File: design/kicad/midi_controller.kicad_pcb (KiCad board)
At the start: 4 copper layers, 166 x 166 mm, 26 parts, among them J1 Conn_01x02_Socket, J2 Conn_01x02_Socket, J3 Conn_01x02_Socket, J4 Conn_01x02_Socket, J5 Conn_01x02_Socket, J6 Conn_01x02_Socket, J7 Conn_01x05, SW1 MIDI_Switch_Pushbutton_PV0H24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, SW2 MIDI_Switch_Pushbutton_PV0H24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, SW3 MIDI_Switch_Pushbutton_PV0H24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

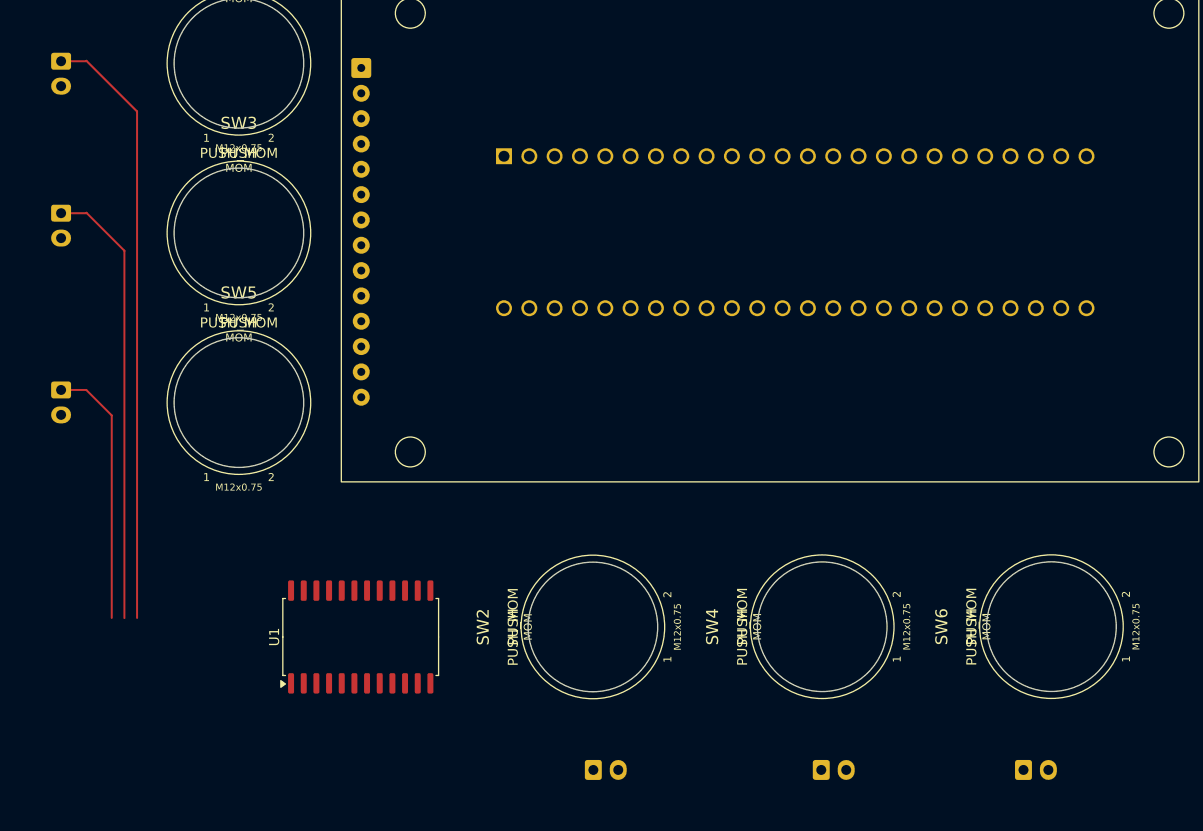
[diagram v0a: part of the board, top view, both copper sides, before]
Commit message: Update kicad binary files
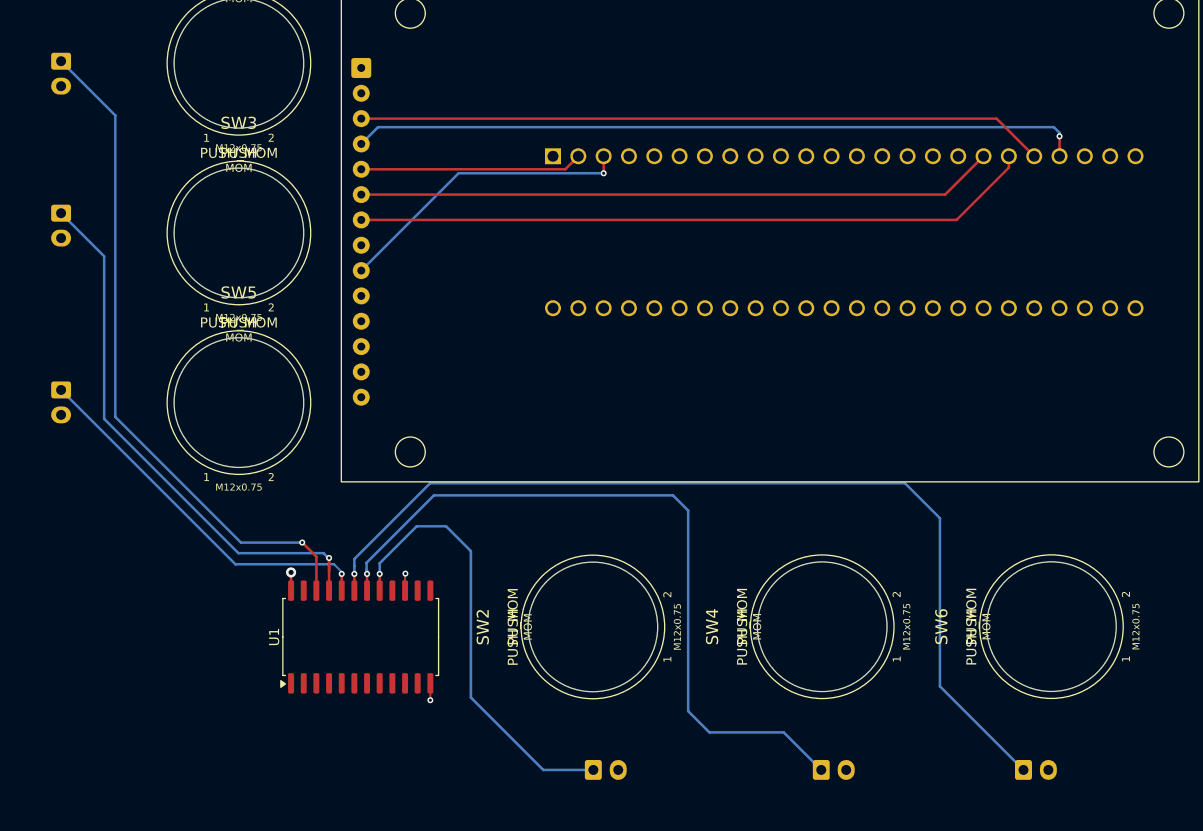
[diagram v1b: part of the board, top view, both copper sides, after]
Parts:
- moved MCU1 4.91 mm to (162.2, 107.5)
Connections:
- ENC_MECH1 pad A: /MIDI_Encoder_Matrix_2x4_with_push_buttons/1x1.QUAD_B -> /MIDI_Encoder_Matrix_2x4_with_push_buttons/1x1.QUAD_A
- ENC_MECH2 pad A: /MIDI_Encoder_Matrix_2x4_with_push_buttons/1x2.QUAD_B -> /MIDI_Encoder_Matrix_2x4_with_push_buttons/1x2.QUAD_A
- ENC_MECH3 pad A: /MIDI_Encoder_Matrix_2x4_with_push_buttons/1x3.QUAD_B -> /MIDI_Encoder_Matrix_2x4_with_push_buttons/1x3.QUAD_A
- ENC_MECH4 pad A: /MIDI_Encoder_Matrix_2x4_with_push_buttons/1x4.QUAD_B -> /MIDI_Encoder_Matrix_2x4_with_push_buttons/1x4.QUAD_A
- ENC_MECH5 pad A: /MIDI_Encoder_Matrix_2x4_with_push_buttons/2x1.QUAD_B -> /MIDI_Encoder_Matrix_2x4_with_push_buttons/2x1.QUAD_A
- ENC_MECH6 pad A: /MIDI_Encoder_Matrix_2x4_with_push_buttons/2x2.QUAD_B -> /MIDI_Encoder_Matrix_2x4_with_push_buttons/2x2.QUAD_A
- ENC_MECH7 pad A: /MIDI_Encoder_Matrix_2x4_with_push_buttons/2x3.QUAD_B -> /MIDI_Encoder_Matrix_2x4_with_push_buttons/2x3.QUAD_A
- ENC_MECH8 pad A: /MIDI_Encoder_Matrix_2x4_with_push_buttons/2x4.QUAD_B -> /MIDI_Encoder_Matrix_2x4_with_push_buttons/2x4.QUAD_A
- J7 pad 2: ENC_A_NAV -> ENC_A_OPT
- J7 pad 3: ENC_B_NAV -> ENC_B_OPT
- MCU1 pad 22: unconnected-(MCU1-30_CRX3-Pad22) -> /Encoder with Push Button_Navigation/QUAD_A
- MCU1 pad 23: unconnected-(MCU1-31_CTX3-Pad23) -> /Encoder with Push Button_Navigation/QUAD_B
- MCU1 pad 24: unconnected-(MCU1-32_OUT1B-Pad24) -> /Encoder with Push Button_Navigation/SW_A
- MCU1 pad 25: ENC_B_NAV -> ENC_A_OPT
- MCU1 pad 26: ENC_A_NAV -> ENC_B_OPT
- MCU1 pad 28: /MIDI_Encoder_Matrix_2x4_with_push_buttons/2x4.QUAD_B -> /MIDI_Encoder_Matrix_2x4_with_push_buttons/1x4.QUAD_B
- MCU1 pad 29: /MIDI_Encoder_Matrix_2x4_with_push_buttons/2x4.QUAD_B -> /MIDI_Encoder_Matrix_2x4_with_push_buttons/1x4.QUAD_A
- MCU1 pad 30: /MIDI_Encoder_Matrix_2x4_with_push_buttons/2x3.QUAD_B -> /MIDI_Encoder_Matrix_2x4_with_push_buttons/2x4.QUAD_B
- MCU1 pad 31: /MIDI_Encoder_Matrix_2x4_with_push_buttons/2x3.QUAD_B -> /MIDI_Encoder_Matrix_2x4_with_push_buttons/2x4.QUAD_A
- MCU1 pad 32: /MIDI_Encoder_Matrix_2x4_with_push_buttons/2x2.QUAD_B -> /MIDI_Encoder_Matrix_2x4_with_push_buttons/1x3.QUAD_A
- MCU1 pad 33: /MIDI_Encoder_Matrix_2x4_with_push_buttons/2x2.QUAD_B -> /MIDI_Encoder_Matrix_2x4_with_push_buttons/1x3.QUAD_B
- MCU1 pad 34: GND -> unconnected-(MCU1-GND-Pad34)
- MCU1 pad 36: /MIDI_Encoder_Matrix_2x4_with_push_buttons/2x1.QUAD_B -> /MIDI_Encoder_Matrix_2x4_with_push_buttons/2x3.QUAD_A
- MCU1 pad 37: /MIDI_Encoder_Matrix_2x4_with_push_buttons/2x1.QUAD_B -> /MIDI_Encoder_Matrix_2x4_with_push_buttons/2x3.QUAD_B
- MCU1 pad 38: /MIDI_Encoder_Matrix_2x4_with_push_buttons/1x4.QUAD_B -> /MIDI_Encoder_Matrix_2x4_with_push_buttons/2x2.QUAD_A
- MCU1 pad 39: /MIDI_Encoder_Matrix_2x4_with_push_buttons/1x4.QUAD_B -> /MIDI_Encoder_Matrix_2x4_with_push_buttons/2x2.QUAD_B
- MCU1 pad 40: /MIDI_Encoder_Matrix_2x4_with_push_buttons/1x3.QUAD_B -> /MIDI_Encoder_Matrix_2x4_with_push_buttons/1x2.QUAD_A
- MCU1 pad 41: /MIDI_Encoder_Matrix_2x4_with_push_buttons/1x3.QUAD_B -> /MIDI_Encoder_Matrix_2x4_with_push_buttons/1x2.QUAD_B
- MCU1 pad 42: /MIDI_Encoder_Matrix_2x4_with_push_buttons/1x2.QUAD_B -> /MIDI_Encoder_Matrix_2x4_with_push_buttons/2x1.QUAD_B
- MCU1 pad 43: /MIDI_Encoder_Matrix_2x4_with_push_buttons/1x2.QUAD_B -> /MIDI_Encoder_Matrix_2x4_with_push_buttons/2x1.QUAD_A
- MCU1 pad 45: /MIDI_Encoder_Matrix_2x4_with_push_buttons/1x1.QUAD_B -> /MIDI_Encoder_Matrix_2x4_with_push_buttons/1x1.QUAD_A
- U1 pad 23: /Encoder with Push Button_Navigation/SW_A -> unconnected-(U1-I8-Pad23)
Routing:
- net +5V: track 0.00 -> 159.7 mm
- net /Buttons_Momentary/BUTTON_PUSH_MOM_04: track 0.00 -> 95.2 mm, vias 0 -> 1
- net /Buttons_Momentary/BUTTON_PUSH_MOM_05: track 0.00 -> 74.4 mm, vias 0 -> 1
- net Net-(D1-RST): track 0.00 -> 73.3 mm, vias 0 -> 1
- net Net-(D1-CS): track 0.00 -> 69.1 mm
- net Net-(D1-SCK): track 0.00 -> 68.3 mm
- net Net-(D1-SDI/MOSI): track 0.00 -> 64.0 mm
- net +3V3: track 0.00 -> 63.8 mm, vias 0 -> 1
- net /Buttons_Momentary/BUTTON_PUSH_MOM_06: track 0.00 -> 44.4 mm, vias 0 -> 1
- net Net-(D1-SDO/MISO): track 0.00 -> 30.1 mm, vias 0 -> 1
- net Net-(D1-DC): track 0.00 -> 22.3 mm
- net /Buttons_Momentary/BUTTON_PUSH_MOM_03: track 26.5 -> 37.6 mm, vias 0 -> 1
- net /Buttons_Momentary/BUTTON_PUSH_MOM_02: track 44.8 -> 54.9 mm, vias 0 -> 1
- net /Buttons_Momentary/BUTTON_PUSH_MOM_01: track 60.5 -> 67.3 mm, vias 0 -> 1
- net GND: track 0.00 -> 3.42 mm, vias 0 -> 2

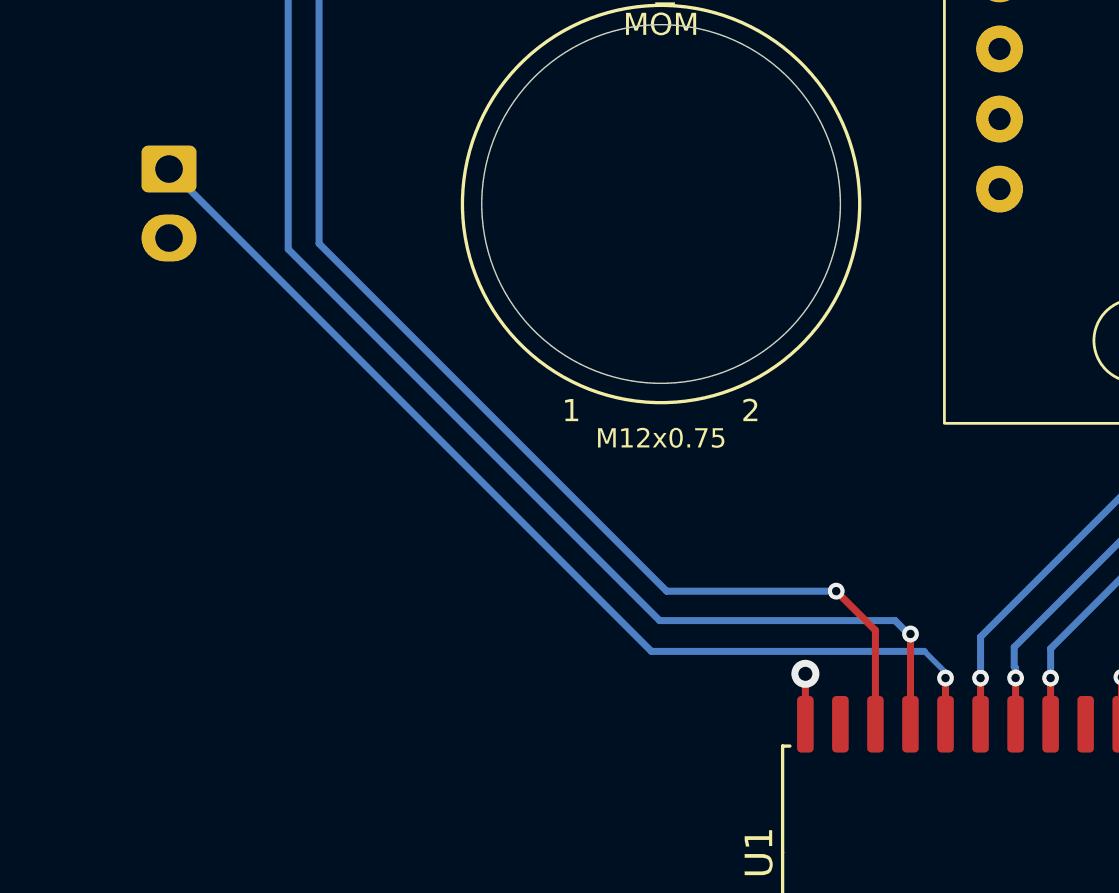
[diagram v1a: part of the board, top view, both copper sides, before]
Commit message: Refactor MIDI controller design files: updated active layer, adjusted hidden nets, and modified junction coordinates in schematic. Enhanced layout for better clarity and organization.
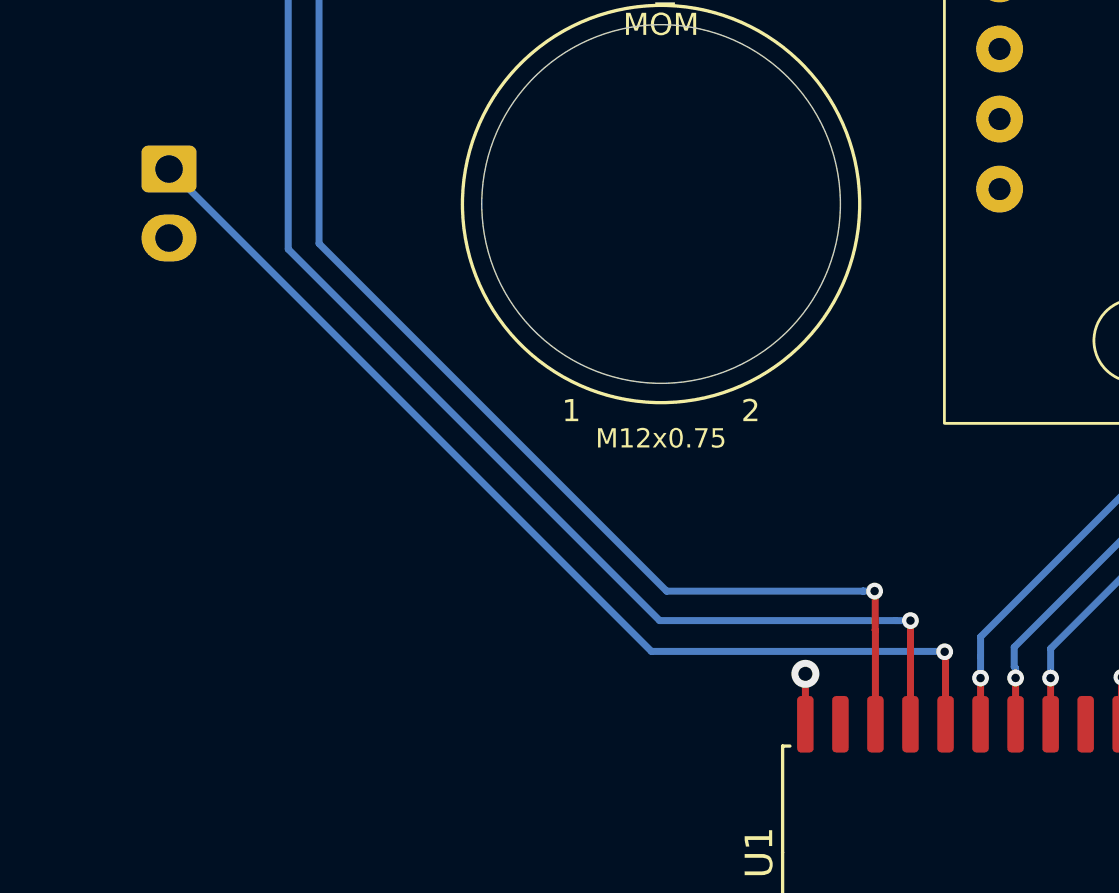
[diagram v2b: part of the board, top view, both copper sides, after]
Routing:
- net /Buttons_Momentary/BUTTON_PUSH_MOM_01: track 67.3 -> 68.1 mm
